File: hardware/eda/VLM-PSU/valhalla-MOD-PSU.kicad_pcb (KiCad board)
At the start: 2 copper layers, 76.2 x 50.8 mm, 21 parts, among them J1 MAINS, J2 DC, J3 BUS, U1 *2

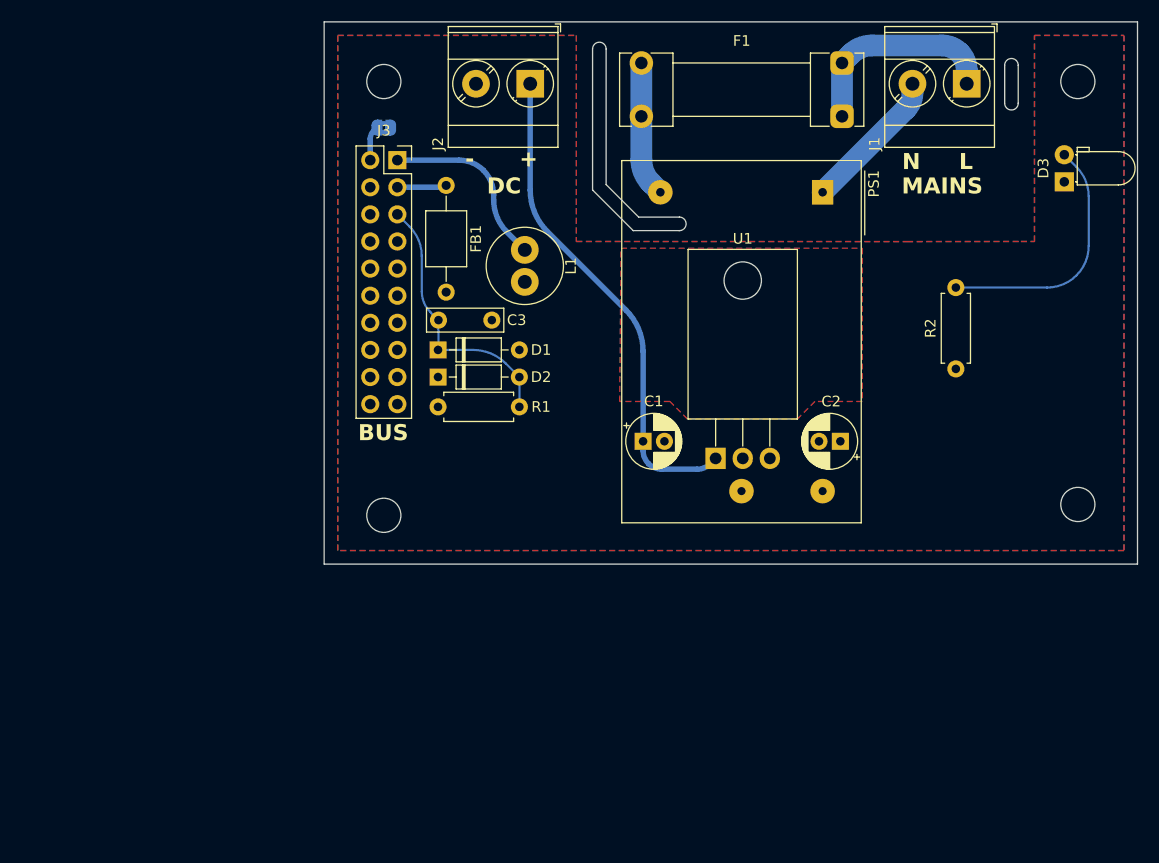
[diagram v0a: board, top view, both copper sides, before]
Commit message: UPDATE: formal dimensions for Valhalla MOD and progrss on CPU
 - added formal dimensions to the Valhalla MOD PSU PCB, to serve as a
   future template and as documentation
 - changed Zener/Schottky symbols to filled variant on same module,
   as customary in the EU
 - solved the Vio independence issue for the UI LEDs on the CPU module
   with a switchable regulator
 - finalized canonical dimensions of the CPU module and placed UI
   LEDs in two rows.
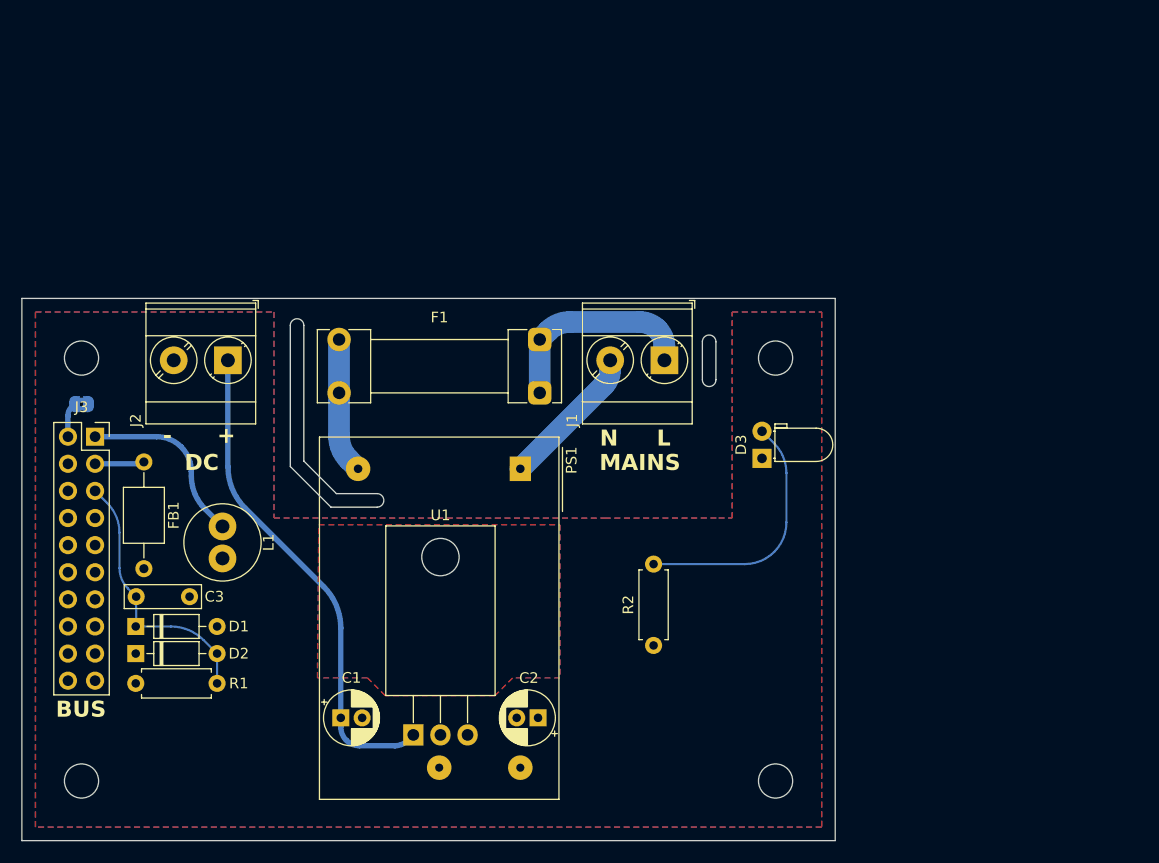
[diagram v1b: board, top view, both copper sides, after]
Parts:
- moved C1 38.4 mm to (67.3, 102.5)
- moved C2 38.4 mm to (85.8, 102.5)
- moved C3 38.4 mm to (48.2, 91.2)
- moved F1 38.4 mm to (86.0, 72.1)
- moved H1 38.4 mm to (43.1, 68.8)
- moved H3 38.4 mm to (108.1, 68.8)
- moved H4 38.4 mm to (108.1, 108.5)
- moved J1 38.4 mm to (97.7, 69.0)
- moved J2 38.4 mm to (56.8, 69.0)
- moved J3 38.4 mm to (44.3, 76.2)
- moved JP1 38.4 mm to (43.1, 73.2)
- moved PS1 38.4 mm to (84.2, 79.2)
- moved R2 38.4 mm to (96.6, 95.8)
- moved U1 38.4 mm to (74.1, 104.1)
- moved D1 38.4 mm to (48.1, 94.0)
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
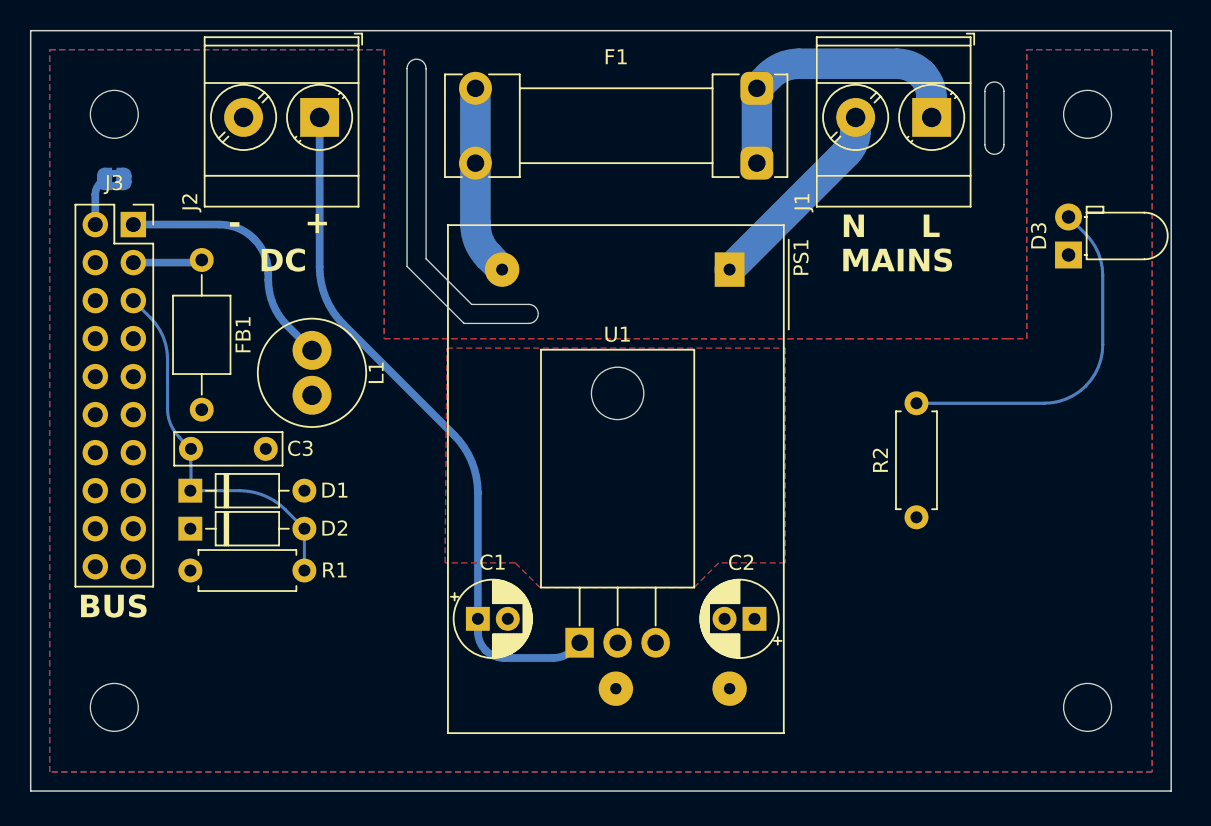
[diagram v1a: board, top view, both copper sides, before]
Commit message: UPDATE: CPU module trace routing complete
 - remaining stuff: crystal dress-up and silkscreen finish-up
 - we may choose not to get artsy on this one (teardrops and curves) due
   to DRC/real estate constraints.
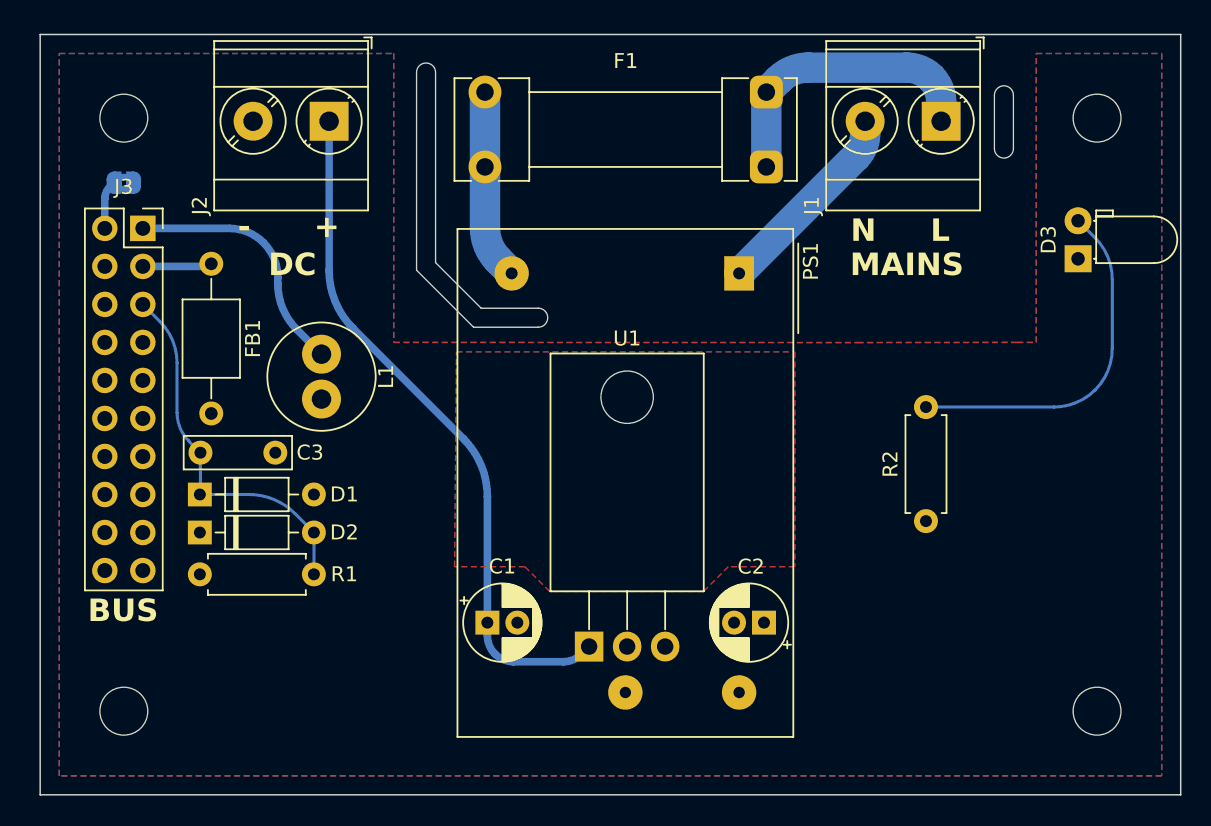
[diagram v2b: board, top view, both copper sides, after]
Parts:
- moved C2 0.68 mm to (86.5, 102.8)
- moved H2 0.68 mm to (43.7, 108.7)
- moved H4 0.68 mm to (108.7, 108.7)
- moved J1 0.68 mm to (98.3, 69.3)
- moved J2 0.68 mm to (57.4, 69.3)
- moved JP1 0.68 mm to (43.7, 73.4)
- moved PS1 0.68 mm to (84.8, 79.5)
- moved H1 0.68 mm to (43.7, 69.1)
- moved H3 0.68 mm to (108.7, 69.1)
- moved D2 0.68 mm to (48.8, 96.8)
- moved L1 0.68 mm to (56.9, 87.9)
- moved R1 0.68 mm to (48.8, 99.6)
- moved C3 0.68 mm to (48.8, 91.4)
- moved D1 0.68 mm to (48.8, 94.2)
- moved FB1 0.68 mm to (49.5, 88.8)
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
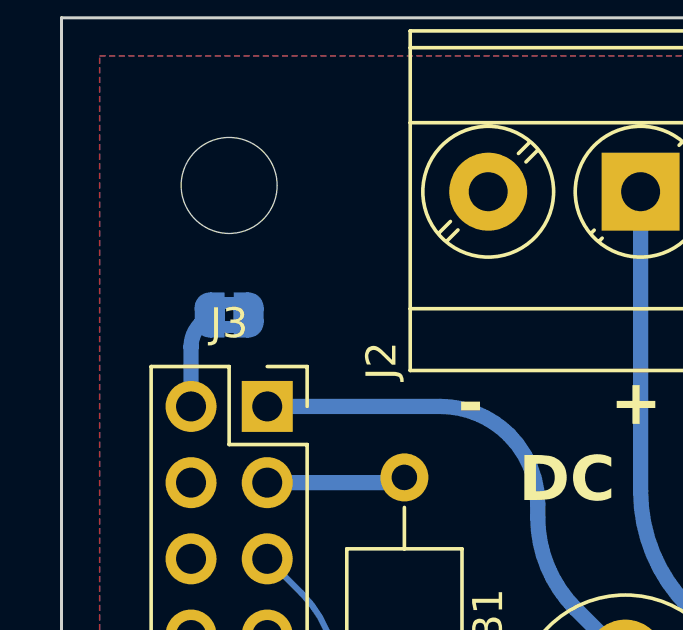
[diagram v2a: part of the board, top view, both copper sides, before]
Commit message: UPDATE: progress towards templatizing dimensions   - used the PSU module as a master copy for now until the template     stabilizes, to be exported as a stand-alone blueprint for future     modules   - minor progress on the CPU(ATMega) module: easier to solder     footprint for LVCC regulator, crystal dress-up and reference     clean-ups.
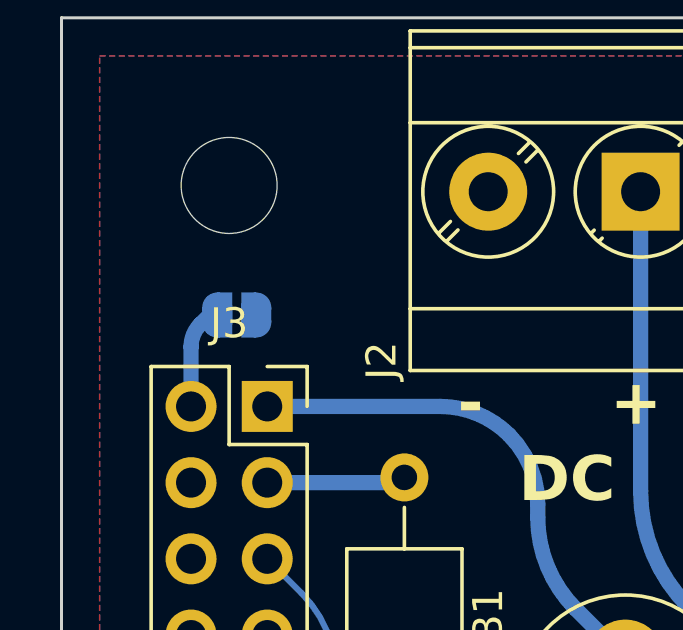
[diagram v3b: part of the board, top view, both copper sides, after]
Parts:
- JP1: value AGND -> *5; footprint Jumper:SolderJumper-2_P1.3mm_Bridged2Bar_RoundedPad1.0x1.5mm -> Jumper:SolderJumper-2_P1.3mm_Open_RoundedPad1.0x1.5mm
- moved JP1 0.25 mm to (43.9, 73.4), turned to 180 degrees
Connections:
- JP1 pad 1: /AGND -> /DGND
- JP1 pad 2: /DGND -> /AGND
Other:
- rule pad_to_mask_clearance: 0 -> 0.0508

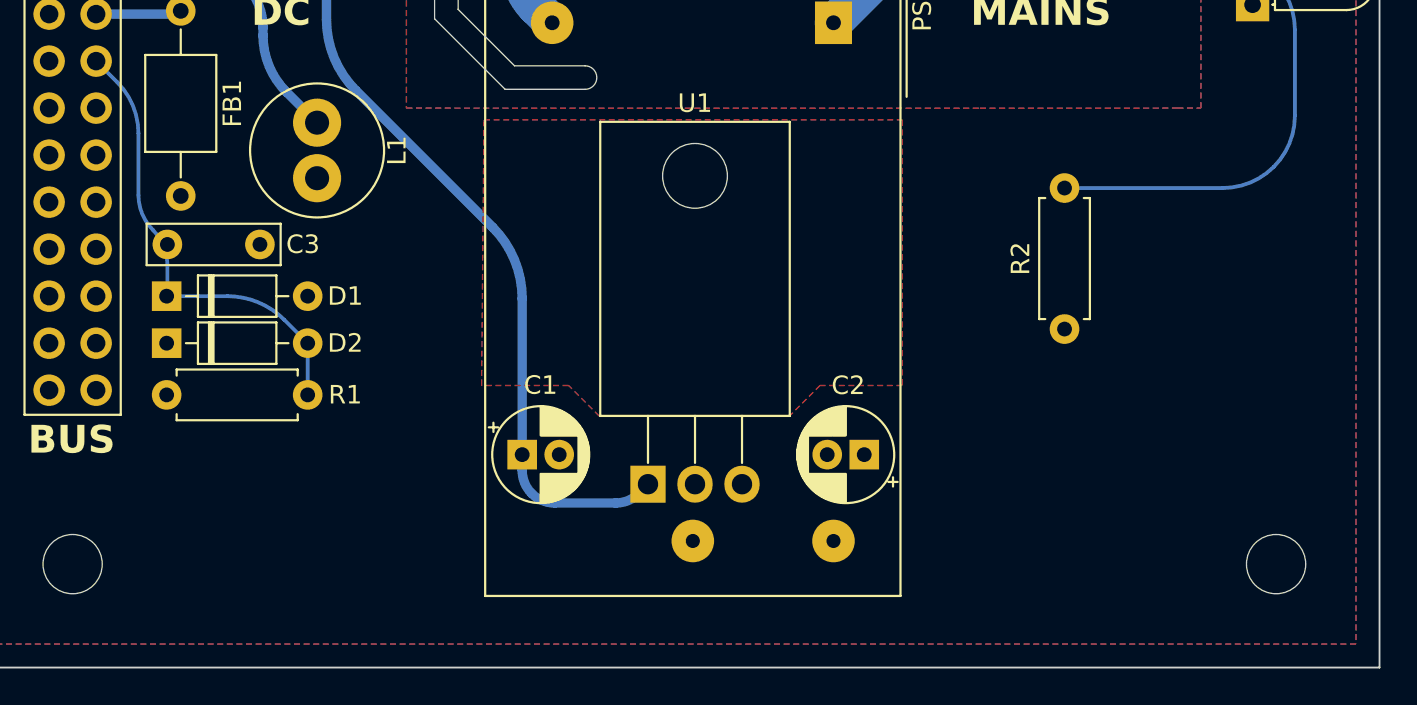
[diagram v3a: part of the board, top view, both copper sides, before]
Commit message: UPDATE: PSU and CPU(ATMega-T) artwork complete
 - also extracted the existing PSU as a template for future modules
 - PSU final touches and RTM
 - CPU(ATMega-T) tied unused inputs to GND, fixed all DRC violations,
   dressed-up silkscreen and RTM.
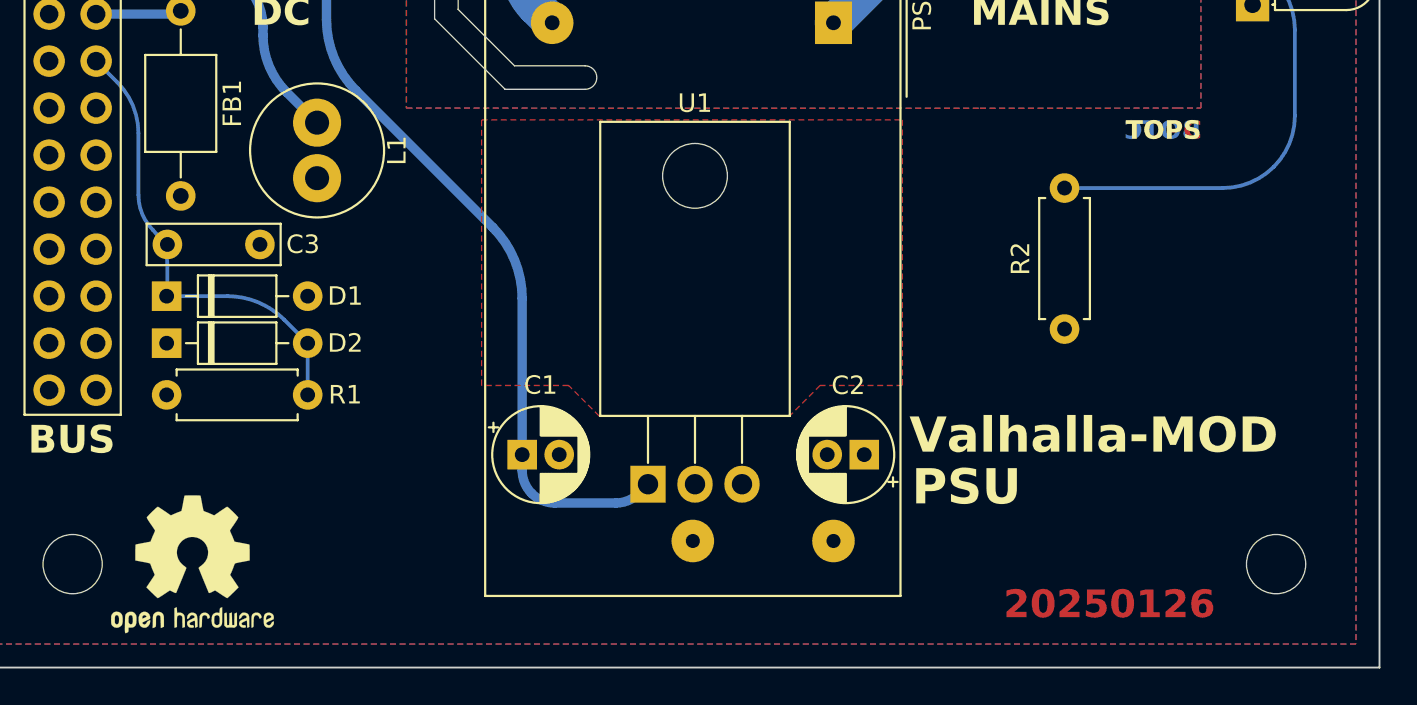
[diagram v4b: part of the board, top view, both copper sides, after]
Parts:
- added REF**: OSHW-Logo2_9.8x8mm_SilkScreen, Symbol:OSHW-Logo2_9.8x8mm_SilkScreen, F.Cu at (50.2, 108.7)
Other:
- board text added: "20250126"
- board text added: "BOTC"
- board text added: "PSU"
- board text added: "TOPC"
- board text added: "TOPS"
- board text added: "Valhalla-MOD"

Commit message: UPDATE: re-touched PSU after latest specification release
  - added LVCC and BVCC and polyfuses on all outputs
  - added simple LVCC control via GPIO
  - layout update to follow.
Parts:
- removed REF**: OSHW-Logo2_9.8x8mm_SilkScreen, Symbol:OSHW-Logo2_9.8x8mm_SilkScreen
- added BT1: CR2032, Battery:Battery_Panasonic_CR2032-VS1N_Vertical_CircularHoles, F.Cu at (71.7, 137.9)
- added F2: *1, Fuse:Fuse_BelFuse_0ZRE0005FF_L8.3mm_W3.8mm, F.Cu at (58.2, 134.5)
- added F3: 100mA, Fuse:Fuse_BelFuse_0ZRE0005FF_L8.3mm_W3.8mm, F.Cu at (58.2, 139.8)
- added F4: 100mA, Fuse:Fuse_BelFuse_0ZRE0005FF_L8.3mm_W3.8mm, F.Cu at (58.2, 145.2)
- added F5: 25mA, Fuse:Fuse_BelFuse_0ZRE0005FF_L8.3mm_W3.8mm, F.Cu at (58.2, 150.5)
- added J4: GPIO, TerminalBlock_Phoenix:TerminalBlock_Phoenix_MPT-0,5-2-2.54_1x02_P2.54mm_Horizontal, F.Cu at (79.0, 150.6)
- added Q1: *3, Package_TO_SOT_THT:TO-92, F.Cu at (67.7, 151.2)
- added R3: 2K2, Resistor_THT:R_Axial_DIN0207_L6.3mm_D2.5mm_P7.62mm_Horizontal, F.Cu at (67.3, 141.9)
- added R4: 10K, Resistor_THT:R_Axial_DIN0207_L6.3mm_D2.5mm_P7.62mm_Horizontal, F.Cu at (67.3, 146.0)
- D1: value *2 -> 5V
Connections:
- net /VCC renamed Net-(D2-K)
- FB1 pad 2: /DVCC -> Net-(F2-Pad1)
- J3 pad 12: unconnected-(J3-Pin_12-Pad12) -> /BVCC
- J3 pad 16: unconnected-(J3-Pin_16-Pad16) -> /LVCC
- L1 pad 2: /AVCC -> Net-(F3-Pad1)

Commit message: UPDATE: MOD-PSU re-layout complete, RTM.
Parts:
- added D4: BAT54, Diode_THT:D_DO-35_SOD27_P7.62mm_Horizontal, F.Cu at (59.2, 97.2)
- F4: value 100mA -> *3
- Q1: footprint Package_TO_SOT_THT:TO-92 -> Package_TO_SOT_THT:TO-92_Inline
- moved F3 60.8 mm to (53.9, 79.2), turned to 180 degrees
- moved F5 52.0 mm to (53.9, 98.8), turned to 180 degrees
- moved F2 51.2 mm to (53.9, 83.5), turned to 180 degrees
- moved Q1 49.2 mm to (64.3, 102.2), turned to 180 degrees
- moved J4 48.5 mm to (52.3, 110.1)
- moved F4 42.3 mm to (53.9, 103.1), turned to 180 degrees
- moved BT1 40.7 mm to (70.2, 97.2), turned to -90 degrees
- moved R4 38.1 mm to (66.8, 107.9), turned to 180 degrees
- moved R3 31.0 mm to (66.8, 110.9), turned to 180 degrees
- moved FB1 18.5 mm to (68.0, 89.3), turned to 180 degrees
- moved U1 12.7 mm to (87.4, 106.1)
- moved C1 12.7 mm to (80.6, 104.5)
- moved C2 12.7 mm to (99.1, 104.5)
- moved PS1 12.7 mm to (97.4, 81.2)
- moved R2 11.9 mm to (107.4, 89.8)
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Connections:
- F4 pad 1: Net-(F4-Pad1) -> Net-(Q1-S)
- F5 pad 1: Net-(BT1-+) -> Net-(D4-K)
- Q1 pad 1: (no net) -> Net-(D2-K)
- Q1 pad 2: (no net) -> Net-(Q1-G)
- Q1 pad 3: (no net) -> Net-(Q1-S)
- R3 pad 1: Net-(Q1-PadG) -> Net-(Q1-G)
- R4 pad 2: Net-(Q1-PadG) -> Net-(Q1-G)
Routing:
- net Net-(D3-A): track 23.9 -> 6.84 mm
- net Net-(Q1-G): track 0.00 -> 16.2 mm
- net /LVCC: track 0.00 -> 14.5 mm
- net /AVCC: track 17.0 -> 4.27 mm
- net Net-(PS1-AC/L): track 12.7 -> 24.6 mm
- net /BVCC: track 0.00 -> 11.6 mm
- net Net-(F3-Pad1): track 0.00 -> 9.41 mm
- net /ILLUMINATION: track 0.00 -> 8.36 mm
- net Net-(Q1-S): track 0.00 -> 8.24 mm
- net Net-(F2-Pad1): track 0.00 -> 7.52 mm
- net Net-(D4-K): track 0.00 -> 5.97 mm
- net Net-(J2-Pin_1): track 46.3 -> 51.7 mm
- net /~{RESET}: track 25.1 -> 19.8 mm
- net Net-(BT1-+): track 0.00 -> 3.41 mm
- net Net-(J1-Pin_1): track 19.8 -> 18.7 mm
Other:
- outline, holes or cut-outs redrawn
- board text added: "20250322"
- board text removed: "20250126"
